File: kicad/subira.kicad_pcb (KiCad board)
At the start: 2 copper layers, 40 x 40 mm, 45 parts, among them J1 USB_C_Receptacle_USB2.0_14P, SW1 SW_Push, U1 ESP32-S3-WROOM-1, U2 AMS1117-3.3, U3 BMI270, U4 LSM9DS1

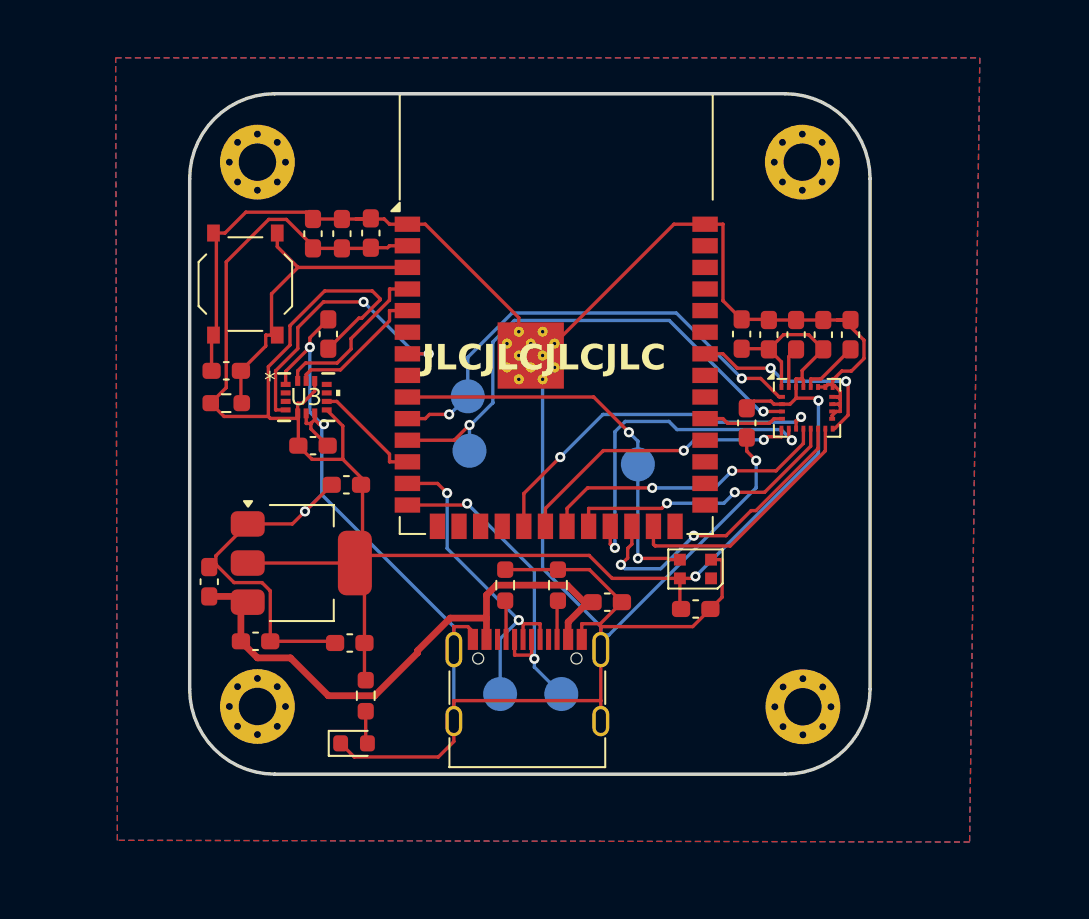
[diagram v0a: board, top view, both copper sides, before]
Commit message: fix: enable usb boot option
Fixes https://github.com/rodneyosodo/subira/issues/2
Fixes https://github.com/rodneyosodo/subira/issues/1
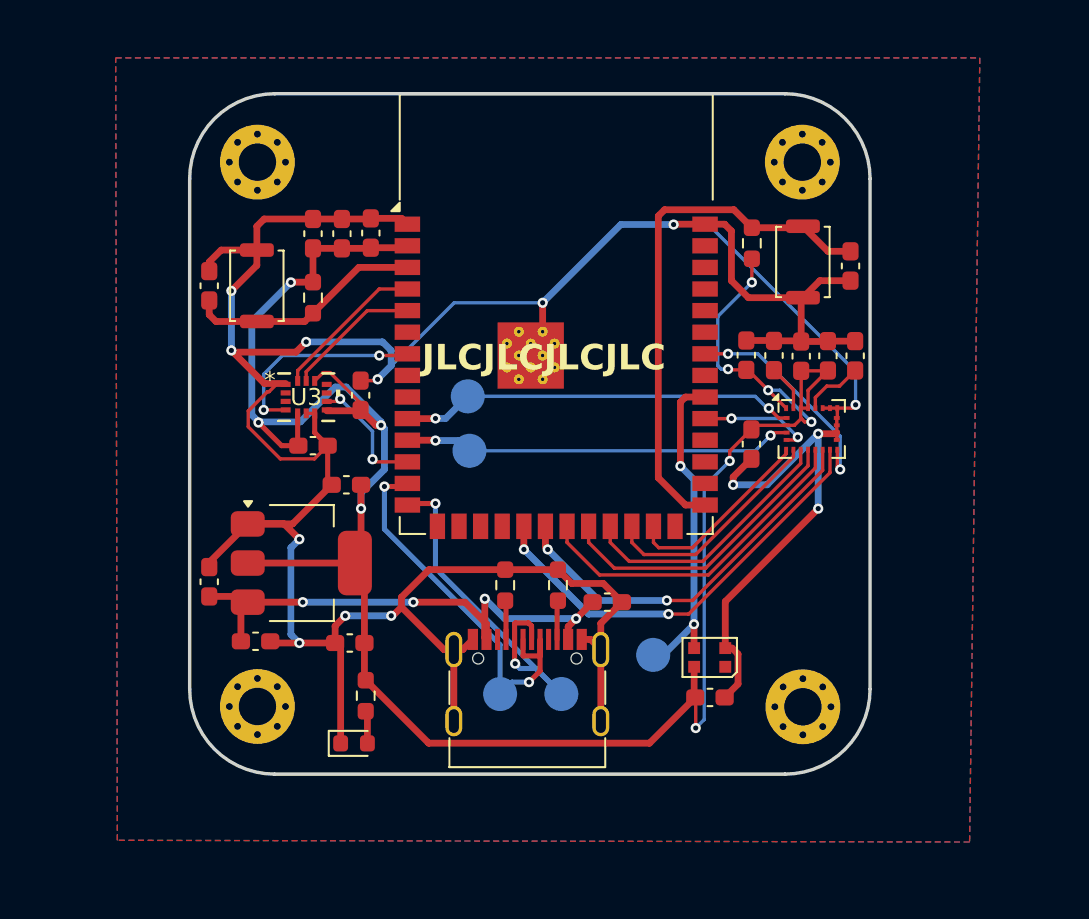
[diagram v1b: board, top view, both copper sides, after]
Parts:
- added C19: 1uF, Capacitor_SMD:C_0603_1608Metric_Pad1.08x0.95mm_HandSolder, F.Cu at (98.0, 58.6)
- added R5: 10K, Resistor_SMD:R_0603_1608Metric_Pad0.98x0.95mm_HandSolder, F.Cu at (92.2, 57.3)
- added SW2: SW_Push, Button_Switch_SMD:SW_Push_SPST_NO_Alps_SKRK, F.Cu at (95.2, 58.4)
- SW1: footprint Button_Switch_SMD:SW_Push_1P1T_XKB_TS-1187A -> Button_Switch_SMD:SW_Push_SPST_NO_Alps_SKRK
- moved kibuzzard-67E73E95 13.0 mm to (86.6, 83.9)
- moved TP1 11.2 mm to (86.4, 81.5)
- moved R1 8.03 mm to (66.4, 60.5), turned to -90 degrees
- moved C10 5.27 mm to (89.7, 84.0)
- moved D2 5.27 mm to (89.7, 81.7)
- moved C1 5.10 mm to (60.3, 59.8), turned to 90 degrees
- moved C18 4.07 mm to (69.2, 66.2)
- moved C17 2.28 mm to (95.1, 63.9)
- moved C14 1.79 mm to (93.5, 63.9)
- moved U4 1.27 mm to (95.7, 68.2)
- moved C13 1.27 mm to (92.2, 69.1)
- moved C15 1.27 mm to (91.9, 63.9)
- moved C12 1.27 mm to (98.3, 63.9)
- moved C16 1.27 mm to (96.7, 63.9)
- moved SW1 0.68 mm to (63.1, 59.8), turned to -90 degrees
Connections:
- U1 pad 19: CS_M -> INT2_A/G
- U1 pad 20: SD0_M -> INT1_A/G
- U1 pad 21: DRDY_M -> INT_M
- U1 pad 22: INT_M -> DRDY_M
- U1 pad 23: CS_A/G -> CS_M
- U1 pad 24: INT1_A/G -> CS_A/G
- U1 pad 25: INT2_A/G -> SD0_M
- U1 pad 27: unconnected-(U1-IO0-Pad27) -> IO0
- U1 pad 32: unconnected-(U1-IO39-Pad32) -> LED
- U1 pad 9: LED -> unconnected-(U1-IO16-Pad9)
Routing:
- net IO0: track 0.00 -> 31.3 mm
- net INT2_A/G: track 14.8 -> 25.7 mm, vias 0 -> 2
- net GND: track 219.8 -> 228.7 mm, vias 4 -> 14
- net +3V3: track 126.4 -> 135.0 mm, vias 2 -> 10
- net LSMSDA: track 30.8 -> 23.0 mm
- net CS_A/G: track 20.1 -> 13.5 mm, vias 2 -> 0
- net SD0_M: track 17.1 -> 11.4 mm, vias 2 -> 0
- net CS_M: track 21.3 -> 15.8 mm, vias 2 -> 0
- net Net-(U1-EN): track 18.9 -> 14.0 mm
- net INT1_A/G: track 18.3 -> 23.2 mm
- net LSMSCL: track 28.0 -> 23.4 mm
- net LED: track 24.0 -> 19.5 mm
- net BM_INT1: track 16.8 -> 12.3 mm
- net D-: track 19.8 -> 24.2 mm
- net D+: track 20.2 -> 23.7 mm
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
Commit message: fix: add labels to RST and BOOT buttons
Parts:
- added kibuzzard-67E8F709: G***, kibuzzard-67E8F709, F.Cu at (63.1, 63.4)
- added kibuzzard-67E8F774: G***, kibuzzard-67E8F774, F.Cu at (92.3, 60.9)
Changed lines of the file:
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@@
+		)
+	)
+	(footprint "kibuzzard-67E8F709"
+		(layer "F.Cu")
+		(at 63.1 63.4)
+		(descr "Generated with KiBuzzard")
+		(tags "kb_params=eyJBbGlnbm1lbnRDaG9pY2UiOiAiQ2VudGVyIiwgIkNhcExlZnRDaG9pY2UiOiAiWyIsICJDYXBSaWdodENob2ljZSI6ICJdIiwgIkZvbnRDb21ib0JveCI6ICJVYnVudHVNb25vLUIiLCAiSGVpZ2h0Q3RybCI6IDEuMCwgIkxheWVyQ29tYm9Cb3giOiAiRi5TaWxrUyIsICJMaW5lU3BhY2luZ0N0cmwiOiAxLjAsICJNdWx0aUxpbmVUZXh0IjogIlJFU0VUIiwgIlBhZGRpbmdCb3R0b21DdHJsIjogMi4wLCAiUGFkZGluZ0xlZnRDdHJsIjogMi4wLCAiUGFkZGluZ1JpZ2h0Q3RybCI6IDIuMCwgIlBhZGRpbmdUb3BDdHJsIjogMi4wLCAiV2lkdGhDdHJsIjogMS4wLCAiYWR2YW5jZWRDaGVja2JveCI6IGZhbHNlLCAiaW5saW5lRm9ybWF0VGV4dGJveCI6IGZhbHNlLCAibGluZW92ZXJTdHlsZUNob2ljZSI6ICJTcXVhcmUiLCAibGluZW92ZXJUaGlja25lc3NDdHJsIjogMX0=")
+		(property "Reference" "kibuzzard-67E8F709"
+			(at 0 -3.839061 0)
+			(layer "F.SilkS")
+			(hide yes)
+			(effects
+				(font
+					(size 0.001 0.001)
+				)
+			)
+		)
+		(property "Value" "G***"
+			(at 0 3.839061 0)
+			(layer "F.SilkS")
+			(hide yes)
+			(effects
+				(font
+					(size 0.001 0.001)
+				)
+			)
+		)
+		(property "Footprint" ""
+			(at 0 0 0)
+			(layer "F.Fab")
+			(hide yes)
+			(effects
+				(font
+					(size 1.27 1.27)
+					(thickness 0.15)
+				)
+			)
+		)
+		(property "Datasheet" ""
+			(at 0 0 0)
+			(layer "F.Fab")
+			(hide yes)
+			(effects
+				(font
+					(size 1.27 1.27)
+					(thickness 0.15)
+				)
+			)
+		)
+		(property "Description" ""
+			(at 0 0 0)
+			(layer "F.Fab")
+			(hide yes)
+			(effects
+				(font
+					(size 1.27 1.27)
+					(thickness 0.15)
+				)
+			)
+		)
+		(attr board_only exclude_from_pos_files exclude_from_bom)
+		(fp_poly
+			(pts
+				(xy -1.521002 -0.184168) (xy -1.533118 -0.252827) (xy -1.569467 -0.300485) (xy -1.625606 -0.328352)
+				(xy -1.697092 -0.337641) (xy -1.724556 -0.336834) (xy -1.756866 -0.332795) (xy -1.756866 -0.03231)
+				(xy -1.713247 -0.03231) (xy -1.625606 -0.042205) (xy -1.566236 -0.07189) (xy -1.521002 -0.184168)
+			)
+			(stroke
+				(width 0)
+				(type solid)
+			)
+			(fill solid)
+			(layer "F.SilkS")
+		)
+		(fp_poly
+			(pts
+				(xy -1.955574 -0.791061) (xy -2.224825 -0.791061) (xy -2.224825 0.791061) (xy -1.955574 0.791061)
+				(xy -1.252827 0.791061) (xy -1.252827 0.500808) (xy -1.461228 0.500808) (xy -1.501414 0.405695)
+				(xy -1.547658 0.314216) (xy -1.598748 0.22395) (xy -1.653473 0.132472) (xy -1.756866 0.132472) (xy -1.756866 0.500808)
+				(xy -1.955574 0.500808) (xy -1.955574 -0.484653) (xy -1.891761 -0.496769) (xy -1.821486 -0.504847)
+				(xy -1.753635 -0.508885) (xy -1.697092 -0.510501) (xy -1.615509 -0.505654) (xy -1.542003 -0.491115)
+				(xy -1.477383 -0.466478) (xy -1.422456 -0.431341) (xy -1.345719 -0.328756) (xy -1.325727 -0.261107)
+				(xy -1.319063 -0.182553) (xy -1.327948 -0.099354) (xy -1.354604 -0.024233) (xy -1.401858 0.038368)
+				(xy -1.472536 0.084006) (xy -1.414378 0.176898) (xy -1.354604 0.283522) (xy -1.298869 0.394992)
+				(xy -1.252827 0.500808) (xy -1.252827 0.791061) (xy -1.133279 0.791061) (xy -1.133279 0.500808)
+				(xy -1.133279 -0.499192) (xy -0.527464 -0.499192) (xy -0.527464 -0.33441) (xy -0.934572 -0.33441)
+				(xy -0.934572 -0.109855) (xy -0.580775 -0.109855) (xy -0.580775 0.054927) (xy -0.934572 0.054927)
+				(xy -0.934572 0.336026) (xy -0.491922 0.336026) (xy -0.491922 0.500808) (xy -1.133279 0.500808)
+				(xy -1.133279 0.791061) (xy -0.052504 0.791061) (xy -0.052504 0.521809) (xy -0.164378 0.515145)
+				(xy -0.251212 0.495153) (xy -0.362682 0.44588) (xy -0.304523 0.28433) (xy -0.200323 0.332795) (xy -0.133078 0.349758)
+				(xy -0.052504 0.355412) (xy 0.030695 0.344911) (xy 0.083199 0.315832) (xy 0.109855 0.273829) (xy 0.117124 0.226171)
+				(xy 0.099354 0.171244) (xy 0.05412 0.128433) (xy -0.00727 0.094507) (xy -0.075121 0.066236) (xy -0.168821 0.029079)
+				(xy -0.256866 -0.024233) (xy -0.322294 -0.1042) (xy -0.348142 -0.22294) (xy -0.325323 -0.348142)
+				(xy -0.256866 -0.442649) (xy -0.188386 -0.486627) (xy -0.104649 -0.513014) (xy -0.005654 -0.521809)
+				(xy 0.080574 -0.516559) (xy 0.155089 -0.500808) (xy 0.270598 -0.453958) (xy 0.212439 -0.300485)
+				(xy 0.122779 -0.339257) (xy 0.008885 -0.355412) (xy -0.07907 -0.342667) (xy -0.131843 -0.304434)
+				(xy -0.149435 -0.240711) (xy -0.133279 -0.189822) (xy -0.092084 -0.15105) (xy -0.035541 -0.121163)
+				(xy 0.026656 -0.096931) (xy 0.124394 -0.057351) (xy 0.218094 0.000808) (xy 0.288368 0.091276) (xy 0.308966 0.152464)
+				(xy 0.315832 0.227787) (xy 0.293013 0.352383) (xy 0.224556 0.445073) (xy 0.153204 0.487704) (xy 0.060851 0.513283)
+				(xy -0.052504 0.521809) (xy -0.052504 0.791061) (xy 0.482229 0.791061) (xy 0.482229 0.500808) (xy 0.482229 -0.499192)
+				(xy 1.088045 -0.499192) (xy 1.088045 -0.33441) (xy 0.680937 -0.33441) (xy 0.680937 -0.109855) (xy 1.034733 -0.109855)
+				(xy 1.034733 0.054927) (xy 0.680937 0.054927) (xy 0.680937 0.336026) (xy 1.123586 0.336026) (xy 1.123586 0.500808)
+				(xy 0.482229 0.500808) (xy 0.482229 0.791061) (xy 1.692246 0.791061) (xy 1.692246 0.500808) (xy 1.491922 0.500808)
+				(xy 1.491922 -0.33441) (xy 1.228595 -0.33441) (xy 1.228595 -0.499192) (xy 1.955574 -0.499192) (xy 1.955574 -0.33441)
+				(xy 1.692246 -0.33441) (xy 1.692246 0.500808) (xy 1.692246 0.791061) (xy 1.955574 0.791061) (xy 2.224825 0.791061)
+				(xy 2.224825 -0.791061) (xy 1.955574 -0.791061) (xy -1.955574 -0.791061)
+			)
+			(stroke
+				(width 0)
+				(type solid)
+			)
+			(fill solid)
+			(layer "F.SilkS")
 		)
 	)
@@
 		)
 	)
+	(footprint "kibuzzard-67E8F774"
+		(layer "F.Cu")
+		(at 92.3 60.9)
+		(descr "Generated with KiBuzzard")
+		(tags "kb_params=eyJBbGlnbm1lbnRDaG9pY2UiOiAiQ2VudGVyIiwgIkNhcExlZnRDaG9pY2UiOiAiWyIsICJDYXBSaWdodENob2ljZSI6ICJdIiwgIkZvbnRDb21ib0JveCI6ICJVYnVudHVNb25vLUIiLCAiSGVpZ2h0Q3RybCI6IDEuMCwgIkxheWVyQ29tYm9Cb3giOiAiRi5TaWxrUyIsICJMaW5lU3BhY2luZ0N0cmwiOiAxLjAsICJNdWx0aUxpbmVUZXh0IjogIkJUIiwgIlBhZGRpbmdCb3R0b21DdHJsIjogMi4wLCAiUGFkZGluZ0xlZnRDdHJsIjogMi4wLCAiUGFkZGluZ1JpZ2h0Q3RybCI6IDIuMCwgIlBhZGRpbmdUb3BDdHJsIjogMi4wLCAiV2lkdGhDdHJsIjogMS4wLCAiYWR2YW5jZWRDaGVja2JveCI6IGZhbHNlLCAiaW5saW5lRm9ybWF0VGV4dGJveCI6IGZhbHNlLCAibGluZW92ZXJTdHlsZUNob2ljZSI6ICJSb3VuZGVkIiwgImxpbmVvdmVyVGhpY2tuZXNzQ3RybCI6IDF9")
+		(property "Reference" "kibuzzard-67E8F774"
+			(at 0 -3.829368 0)
+			(layer "F.SilkS")
+			(hide yes)
+			(effects
+				(font
+					(size 0.001 0.001)
+				)
+			)
+		)
+		(property "Value" "G***"
+			(at 0 3.829368 0)
+			(layer "F.SilkS")
+			(hide yes)
+			(effects
+				(font
+					(size 0.001 0.001)
+				)
+			)
+		)
+		(property "Footprint" ""
+			(at 0 0 0)
+			(layer "F.Fab")
+			(hide yes)
+			(effects
+				(font
+					(size 1.27 1.27)
+					(thickness 0.15)
+				)
+			)
+		)
+		(property "Datasheet" ""
+			(at 0 0 0)
+			(layer "F.Fab")
+			(hide yes)
+			(effects
+				(font
+					(size 1.27 1.27)
+					(thickness 0.15)
+				)
+			)
+		)
+		(property "Description" ""
+			(at 0 0 0)
+			(layer "F.Fab")
+			(hide yes)
+			(effects
+				(font
+					(size 1.27 1.27)
+					(thickness 0.15)
+				)
+			)
+		)
+		(attr board_only exclude_from_pos_files exclude_from_bom)
+		(fp_poly
+			(pts
+				(xy -0.545234 0.061389) (xy -0.545234 0.332795) (xy -0.499192 0.337641) (xy -0.449919 0.339257)
+				(xy -0.383683 0.333603) (xy -0.326333 0.312601) (xy -0.285137 0.268982) (xy -0.268982 0.197092)
+				(xy -0.315024 0.092892) (xy -0.438611 0.061389) (xy -0.545234 0.061389)
+			)
+			(stroke
+				(width 0)
+				(type solid)
+			)
+			(fill solid)
+			(layer "F.SilkS")
+		)
+		(fp_poly
+			(pts
+				(xy -0.46769 -0.103393) (xy -0.352989 -0.136511) (xy -0.314216 -0.227787) (xy -0.325525 -0.285137)
+				(xy -0.35622 -0.319063) (xy -0.401454 -0.335218) (xy -0.454766 -0.339257) (xy -0.501616 -0.337641)
+				(xy -0.545234 -0.332795) (xy -0.545234 -0.103393) (xy -0.46769 -0.103393)
+			)
+			(stroke
+				(width 0)
+				(type solid)
+			)
+			(fill solid)
+			(layer "F.SilkS")
+		)
+		(fp_poly
+			(pts
+				(xy -0.743942 -0.781368) (xy -1.013193 -0.781368) (xy -1.013193 0.781368) (xy -0.743942 0.781368)
+				(xy -0.466074 0.781368) (xy -0.466074 0.512116) (xy -0.533522 0.510299) (xy -0.603393 0.504847)
+				(xy -0.674071 0.495759) (xy -0.743942 0.483037) (xy -0.743942 -0.487884) (xy -0.619548 -0.504847)
+				(xy -0.48546 -0.512116) (xy -0.382876 -0.50626) (xy -0.301292 -0.488691) (xy -0.189822 -0.427302)
+				(xy -0.134895 -0.342488) (xy -0.120355 -0.248788) (xy -0.129039 -0.181745) (xy -0.155089 -0.122779)
+				(xy -0.247981 -0.035541) (xy -0.162561 0.008078) (xy -0.109855 0.06462) (xy -0.082593 0.129241)
+				(xy -0.073506 0.197092) (xy -0.081179 0.280089) (xy -0.1042 0.348142) (xy -0.187399 0.445073) (xy -0.24475 0.476171)
+				(xy -0.311793 0.496769) (xy -0.386309 0.508279) (xy -0.466074 0.512116) (xy -0.466074 0.781368)
+				(xy 0.480614 0.781368) (xy 0.480614 0.499192) (xy 0.280291 0.499192) (xy 0.280291 -0.336026) (xy 0.016963 -0.336026)
+				(xy 0.016963 -0.500808) (xy 0.743942 -0.500808) (xy 0.743942 -0.336026) (xy 0.480614 -0.336026)
+				(xy 0.480614 0.499192) (xy 0.480614 0.781368) (xy 0.743942 0.781368) (xy 1.013193 0.781368) (xy 1.013193 -0.781368)
+				(xy 0.743942 -0.781368) (xy -0.743942 -0.781368)
+			)
+			(stroke
+				(width 0)
+				(type solid)
+			)
+			(fill solid)
+			(layer "F.SilkS")
+		)
+	)

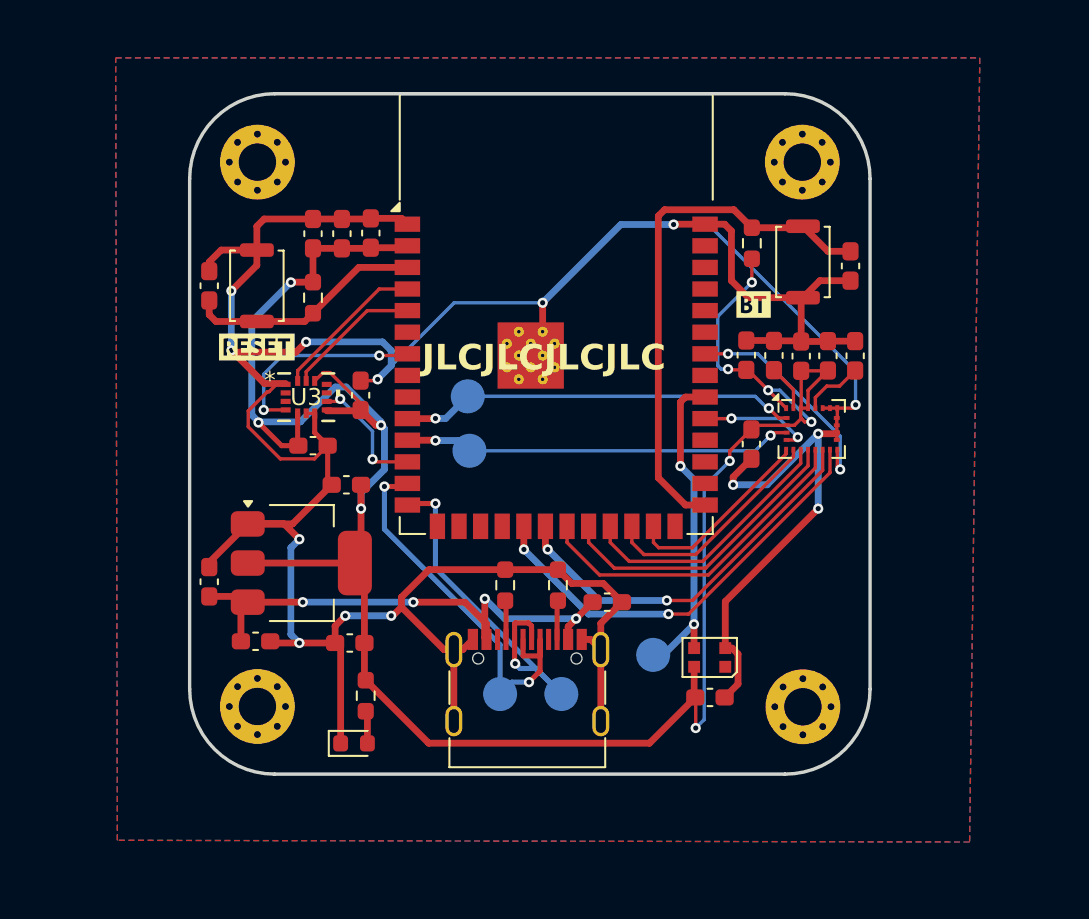
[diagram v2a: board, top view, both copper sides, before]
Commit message: fix(schematic): add 5.1K pull up resistors
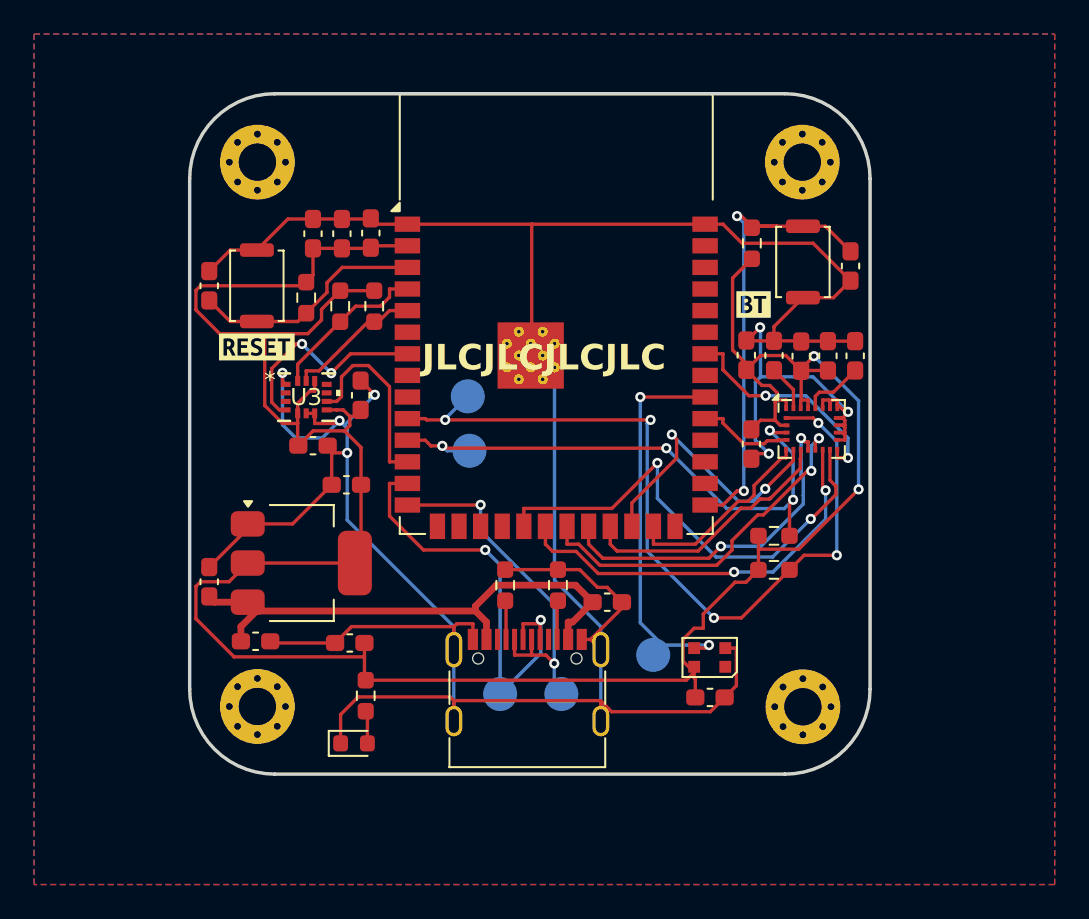
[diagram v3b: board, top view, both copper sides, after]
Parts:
- added R6: 5.1K, Resistor_SMD:R_0603_1608Metric_Pad0.98x0.95mm_HandSolder, F.Cu at (93.5, 74.5)
- added R7: 5.1K, Resistor_SMD:R_0603_1608Metric_Pad0.98x0.95mm_HandSolder, F.Cu at (93.5, 76.5)
- added R8: 5.1K, Resistor_SMD:R_0603_1608Metric_Pad0.98x0.95mm_HandSolder, F.Cu at (68.0, 61.0)
- added R9: 5.1K, Resistor_SMD:R_0603_1608Metric_Pad0.98x0.95mm_HandSolder, F.Cu at (70.0, 61.0)
- moved R2 0.40 mm to (66.0, 60.5)
- renumbered C19 to C1, C9 to C10, C10 to C11, C11 to C12, C12 to C13, C13 to C14, C14 to C15, C15 to C16, C16 to C17, C17 to C18, C18 to C19, C1 to C2, C2 to C3, C3 to C4, C4 to C5, C5 to C6, C6 to C7, C7 to C8, C8 to C9, R5 to R1, R1 to R2, R2 to R3, R3 to R4, R4 to R5, SW2 to SW1, SW1 to SW2
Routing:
- net LSMSCL: track 23.4 -> 48.6 mm, vias 2 -> 5
- net +3V3: track 135.0 -> 151.5 mm, vias 10 -> 2
- net LSMSDA: track 23.0 -> 34.2 mm, vias 2 -> 4
- net BM_INT2: track 7.30 -> 11.2 mm, vias 2 -> 0
- net LED: track 19.5 -> 23.4 mm
- net GND: track 228.7 -> 224.9 mm, vias 14 -> 7
- net CS_A/G: track 13.5 -> 17.0 mm, vias 0 -> 2
- net IO0: track 31.3 -> 28.0 mm, vias 0 -> 2
- net INT2_A/G: track 25.7 -> 28.3 mm
- net D-: track 24.2 -> 26.7 mm
- net DRDY_M: track 17.9 -> 20.2 mm, vias 0 -> 2
- net D+: track 23.7 -> 21.8 mm
- net INT_M: track 20.0 -> 21.4 mm, vias 0 -> 2
- net SD0_A/G: track 6.63 -> 5.65 mm, vias 2 -> 0
- net INT1_A/G: track 23.2 -> 23.7 mm
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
